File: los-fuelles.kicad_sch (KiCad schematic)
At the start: 18 parts, among them J1 PWR, J2 PWR, J3 Stomp, Q1 MMBFJ201, Q2 MPSA13

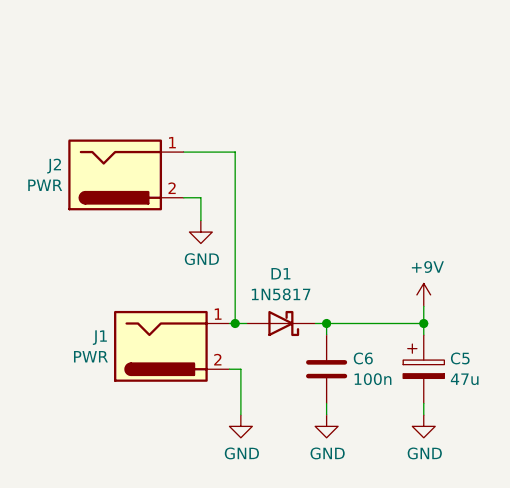
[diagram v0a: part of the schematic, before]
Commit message: updated to KiCad 6.0
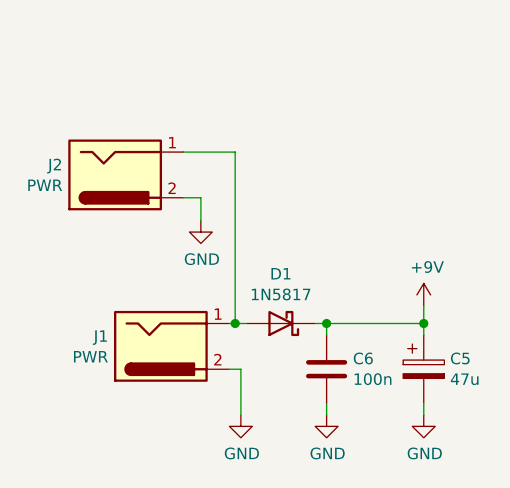
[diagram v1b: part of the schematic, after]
